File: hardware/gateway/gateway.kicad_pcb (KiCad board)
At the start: 2 copper layers, 124 x 36 mm, 73 parts, among them IC1 STM8L151K4T6, IC2 CC1101RGPR, IC3 LT1615ES5-1#TRMPBF, IC4 MIC4427YM, IC5 MB85RC64TAPNF-G-BDERE1, J1 G8250041000YEU, J2 M20-9770342, Q1 IRLML6402TRPBF, U1 2462, Y1 NX3225GA-26.000M-STD-CRG-2

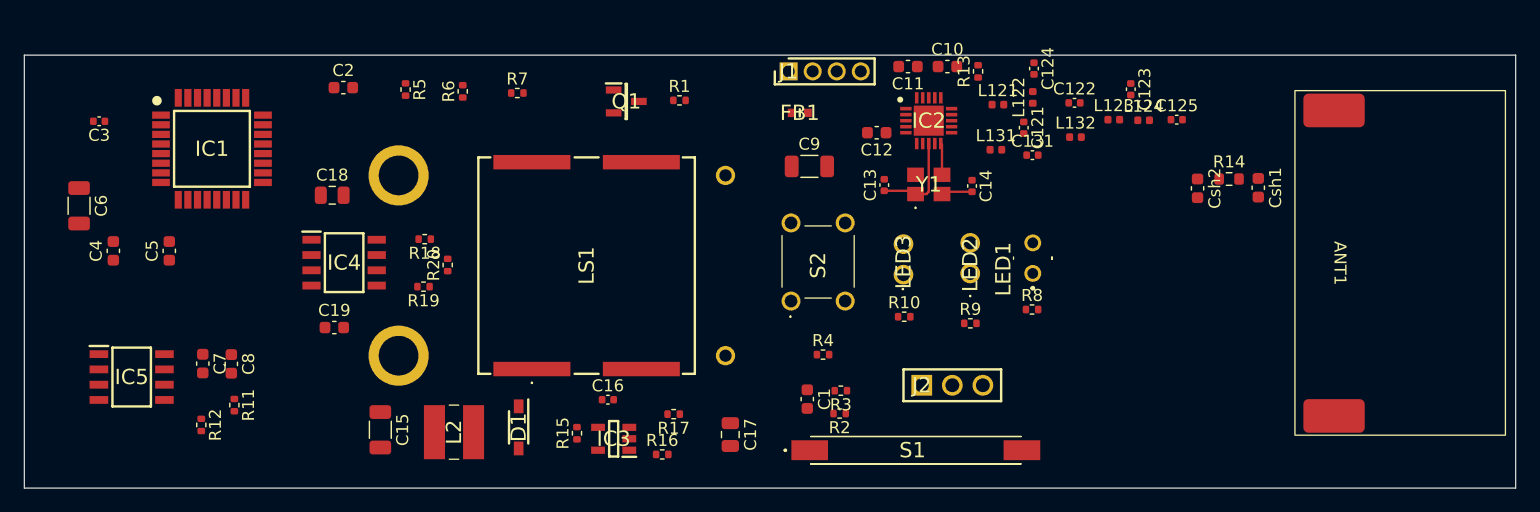
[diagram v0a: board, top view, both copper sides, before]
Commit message: EG-12 Adaption of components places.
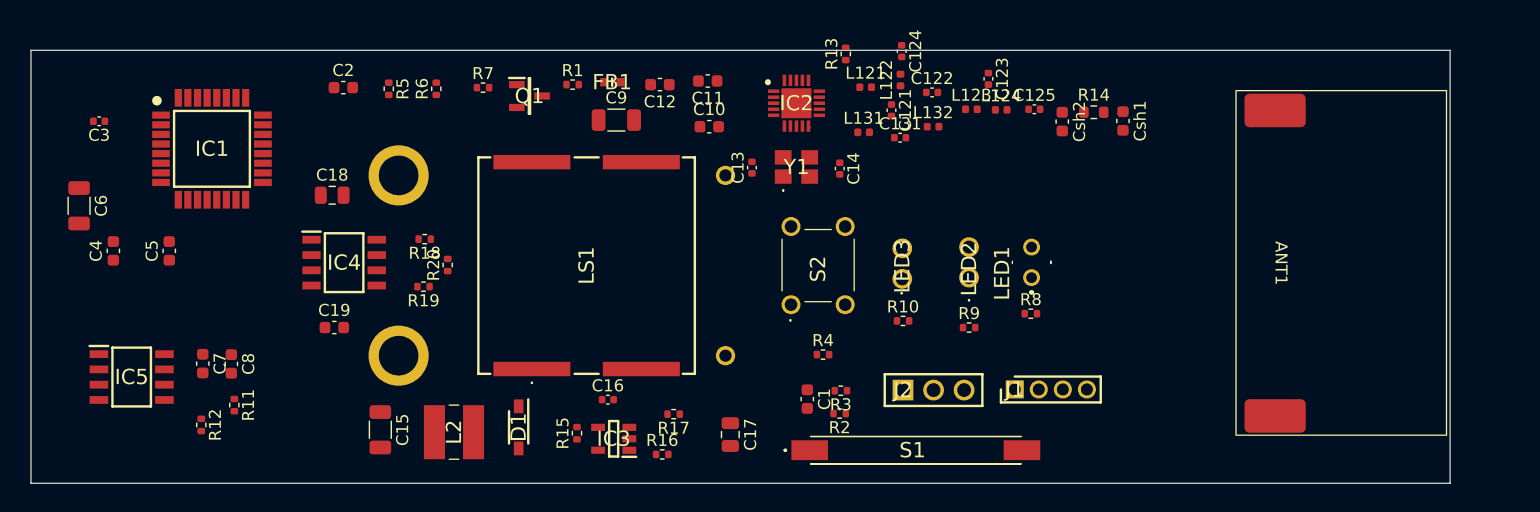
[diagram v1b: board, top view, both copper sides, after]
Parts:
- moved J1 32.5 mm to (161.2, 153.0)
- moved C10 20.4 mm to (135.8, 131.2)
- moved C12 18.5 mm to (131.7, 127.7)
- moved C11 16.7 mm to (135.6, 127.3)
- moved C9 16.5 mm to (128.0, 130.6)
- moved FB1 15.8 mm to (127.7, 127.5)
- moved Csh2 12.5 mm to (165.1, 130.7)
- moved R14 12.5 mm to (167.7, 129.9)
- moved Csh1 12.5 mm to (170.2, 130.7)
- moved C125 11.9 mm to (162.8, 129.7)
- moved L123 11.9 mm to (157.5, 129.7)
- moved L124 11.9 mm to (160.0, 129.8)
- moved C122 11.9 mm to (154.3, 128.3)
- moved C123 11.9 mm to (159.0, 127.2)
- moved L132 11.9 mm to (154.4, 131.2)
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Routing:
- net Net-(IC2-XOSC_Q1): track 7.89 -> 0.38 mm
- net Net-(IC2-XOSC_Q2): track 2.64 -> 0.14 mm
- net GND: track 2.58 -> 0.27 mm
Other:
- board size 124 x 36 mm -> 118 x 36 mm

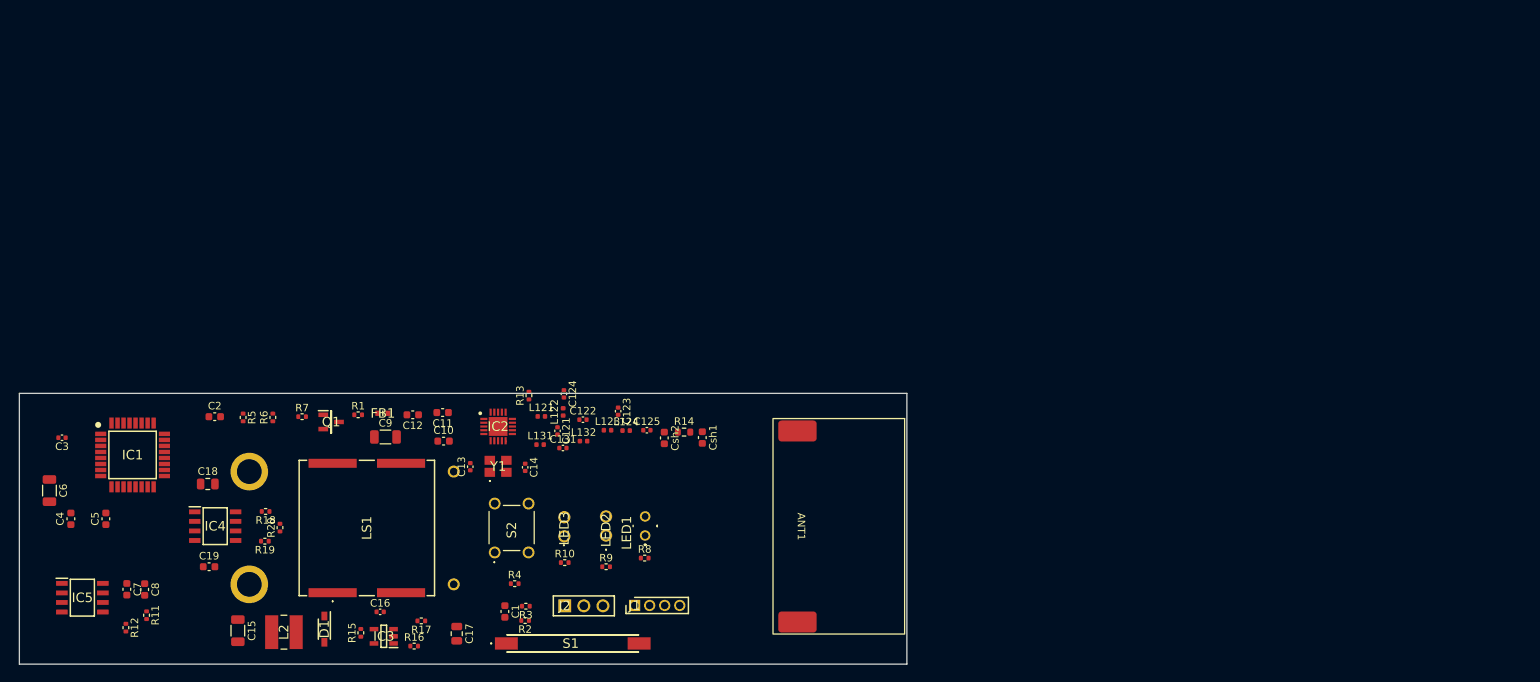
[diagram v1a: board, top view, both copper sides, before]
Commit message: EG-12 All components placed. RF connected, except antenna. Buzzer connected, buzzer power supply connected, FRAM connected. Majority os MCU connections  missing.
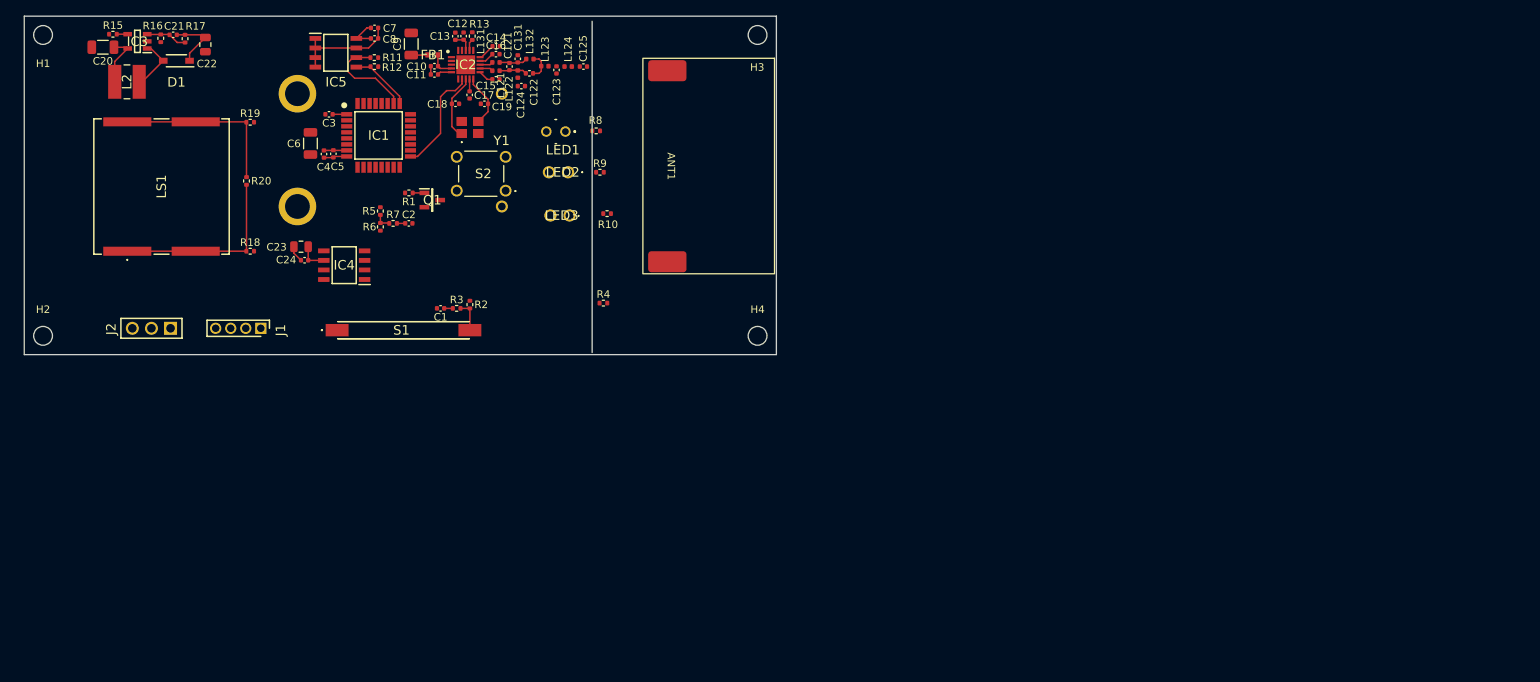
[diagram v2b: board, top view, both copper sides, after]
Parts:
- removed the C19 at (104.6, 147.8)
- removed Csh1, Csh2: 0, Capacitor_SMD:C_0603_1608Metric
- removed R14: 0R, Resistor_SMD:R_0603_1608Metric
- added C13: 1uF, Capacitor_SMD:C_0402_1005Metric, F.Cu at (137.3, 77.3)
- added C14: 100nF, Capacitor_SMD:C_0402_1005Metric, F.Cu at (142.7, 78.7)
- added C15: 100nF, Capacitor_SMD:C_0402_1005Metric, F.Cu at (142.7, 83.0)
- added C16: 100nF, Capacitor_SMD:C_0402_1005Metric, F.Cu at (142.7, 79.7)
- added C17: 100nF, Capacitor_SMD:C_0402_1005Metric, F.Cu at (139.2, 85.1)
- added C24: 100nF, Capacitor_SMD:C_0402_1005Metric, F.Cu at (117.3, 107.1)
- added H1: MountingHole, MountingHole:MountingHole_2.5mm, F.Cu at (82.5, 77.2)
- added H2: MountingHole, MountingHole:MountingHole_2.5mm, F.Cu at (82.5, 117.2)
- added H3: MountingHole, MountingHole:MountingHole_2.5mm, F.Cu at (177.5, 77.2)
- added H4: MountingHole, MountingHole:MountingHole_2.5mm, F.Cu at (177.5, 117.2)
- C1, C11, C12, C2, C4, C5, C7, C8: footprint Capacitor_SMD:C_0603_1608Metric -> Capacitor_SMD:C_0402_1005Metric
- C10: value 1uF -> 100nF; footprint Capacitor_SMD:C_0603_1608Metric -> Capacitor_SMD:C_0402_1005Metric
- moved R16 87.6 mm to (98.2, 77.6), turned to 90 degrees
- moved R15 86.1 mm to (91.8, 77.0), turned to 0 degrees
- moved IC3 85.6 mm to (95.0, 78.0)
- moved C22 85.2 mm to (104.1, 78.4)
- moved R17 83.5 mm to (101.4, 77.6), turned to 90 degrees
- moved C7 81.6 mm to (126.6, 76.2), turned to 0 degrees
- moved R12 81.6 mm to (126.5, 81.4), turned to 0 degrees
- moved C21 81.5 mm to (99.8, 77.1), turned to 180 degrees
- moved R11 80.1 mm to (126.5, 80.2), turned to 0 degrees
- moved IC5 79.9 mm to (121.4, 79.5)
- moved C20 79.6 mm to (90.5, 78.8), turned to 180 degrees
- moved C8 79.4 mm to (126.6, 77.6), turned to 0 degrees
- moved D1 78.1 mm to (100.2, 80.6), turned to 180 degrees
- moved L2 76.1 mm to (93.7, 83.4), turned to -90 degrees
- moved J2 64.1 mm to (99.5, 116.2), turned to 180 degrees
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- renumbered C13 to C18, C14 to C19, C15 to C20, C16 to C21, C17 to C22, C18 to C23
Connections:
- C11 pad 1: RF_VDD -> Net-(IC2-DCOUPL)
- C12 pad 1: Net-(IC2-DCOUPL) -> RF_VDD
- C125 pad 2: Net-(C125-Pad2) -> /RF/RF_LINE
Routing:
- net Net-(LS1-+_1): track 0.00 -> 24.7 mm
- net Net-(LS1--_1): track 0.00 -> 23.2 mm
- net GND: track 0.27 -> 20.4 mm
- net VDD: track 0.00 -> 16.8 mm
- net /MCU/CS: track 0.00 -> 14.4 mm
- net RF_VDD: track 0.00 -> 14.0 mm
- net SCL: track 0.00 -> 12.8 mm
- net +12V: track 0.00 -> 11.8 mm
- net SDA: track 0.00 -> 8.42 mm
- net Net-(IC2-XOSC_Q1): track 0.38 -> 8.79 mm
- net Net-(D1-A): track 0.00 -> 7.16 mm
- net Net-(IC2-XOSC_Q2): track 0.14 -> 7.00 mm
- net Net-(IC3-FB): track 0.00 -> 5.54 mm
- net Net-(R2-Pad1): track 0.00 -> 4.14 mm
- net Net-(C121-Pad2): track 0.00 -> 3.79 mm
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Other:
- board size 118 x 36 mm -> 100 x 45 mm

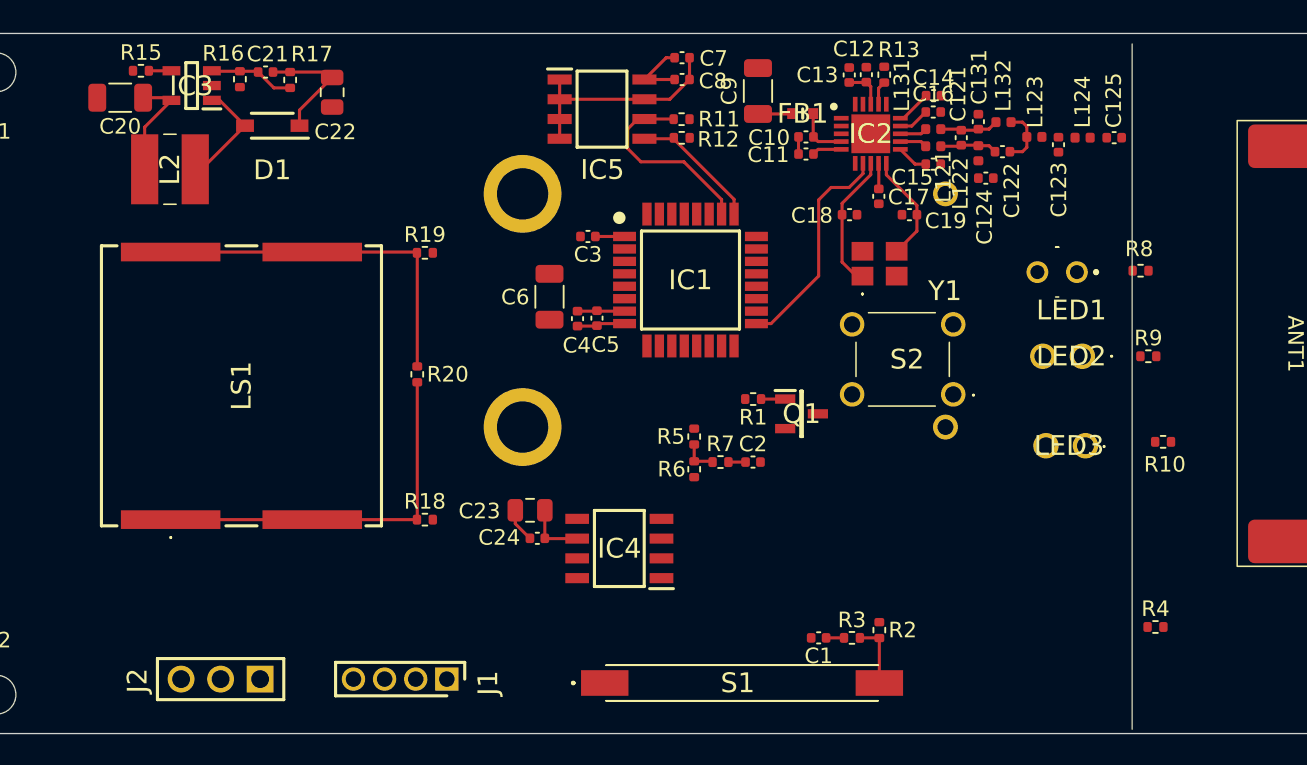
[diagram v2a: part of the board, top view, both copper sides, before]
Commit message: EG-12 All components connected, except antenna and ground plane.
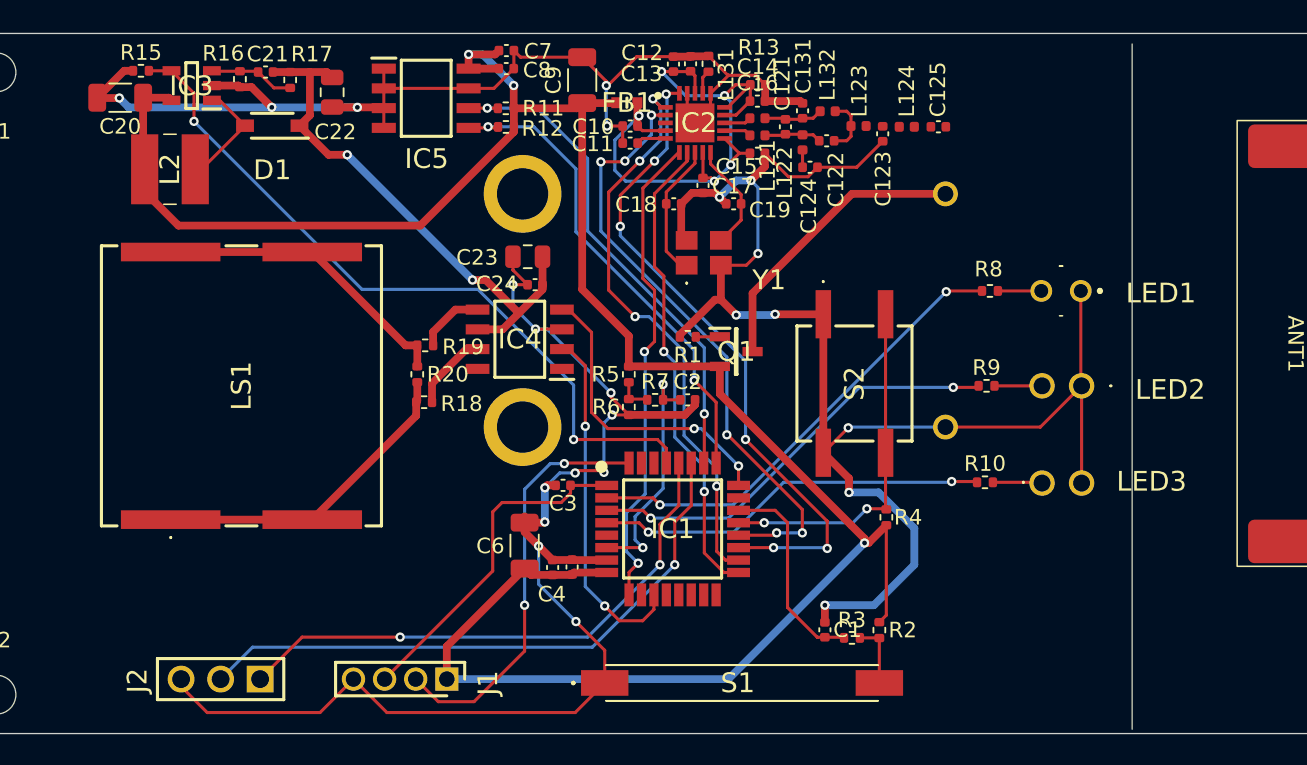
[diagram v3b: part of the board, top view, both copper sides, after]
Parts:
- S2: value B3F-1070 -> TL6120DF160QG; footprint MyParts:B3F1060 -> MyParts:TL6120DF160QG
- moved R4 18.7 mm to (139.7, 105.8), turned to -90 degrees
- moved C23 16.3 mm to (116.7, 89.0)
- moved C24 16.3 mm to (117.1, 90.8)
- moved C3 16.1 mm to (118.9, 103.7)
- moved C4 16.1 mm to (118.2, 109.0)
- moved C5 16.1 mm to (119.5, 108.9)
- moved C6 16.1 mm to (116.5, 107.6)
- moved IC1 16.0 mm to (126.0, 106.5)
- moved IC4 14.9 mm to (116.1, 94.3)
- moved R10 11.7 mm to (146.0, 103.5)
- moved C124 11.3 mm to (134.8, 83.2)
- moved C14 11.3 mm to (131.4, 78.0)
- moved C15 11.3 mm to (131.4, 82.3)
- moved C16 11.3 mm to (131.4, 79.0)
- moved C18 11.3 mm to (126.0, 85.6)
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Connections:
- S2 pad 1: BTN -> GND
- S2 pad 2: BTN -> GND
- S2 pad 3: GND -> BTN
- S2 pad 4: GND -> BTN
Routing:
- net GND: track 20.4 -> 257.3 mm, vias 0 -> 23
- net VDD: track 16.8 -> 147.5 mm, vias 0 -> 3
- net /Buzzer/BZR_EN: track 1.45 -> 47.4 mm, vias 0 -> 2
- net /MCU/SDI: track 0.00 -> 42.6 mm, vias 0 -> 6
- net /MCU/SDO: track 0.00 -> 39.5 mm, vias 0 -> 6
- net RX: track 0.00 -> 39.2 mm, vias 0 -> 1
- net /MCU/SCLK: track 0.00 -> 36.8 mm, vias 0 -> 4
- net TX: track 0.00 -> 35.8 mm, vias 0 -> 2
- net /MCU/IRQ: track 0.00 -> 31.1 mm, vias 0 -> 2
- net LED_B: track 0.00 -> 30.0 mm, vias 0 -> 2
- net LED_Y: track 0.00 -> 27.6 mm, vias 0 -> 2
- net RF_VDD: track 14.0 -> 41.2 mm, vias 0 -> 5
- net SWIM: track 0.00 -> 26.8 mm, vias 0 -> 2
- net LED_R: track 0.00 -> 25.4 mm, vias 0 -> 2
- net SDA: track 8.42 -> 31.4 mm, vias 0 -> 2
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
